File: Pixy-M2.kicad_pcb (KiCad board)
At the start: 4 copper layers, 66 x 100 mm, 78 parts, among them J1 USB_C_Receptacle_USB2.0_14P, J10 SM09B-SRSS-TB, J11 SM06B-SRSS-TB, J4 SM06B-SRSS-TB, J5 SM06B-SRSS-TB, J6 SM06B-SRSS-TB, J7 SM06B-SRSS-TB, J8 S6B-PH-K, J9 S6B-PH-K, Q1 AO4407A, SW1 SW_Push, SW2 SW_Push, SW3 JS102011SAQN, U1 ESP32-S3-WROOM-1-N16, U2 USBLC6-2SC6, U3 AP63203WU, U4 DRV8231ADSG, U5 DRV8231ADSG

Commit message: layout: shorten GPIO48 encoder route for audit P3
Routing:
- net /GPIO48: track 72.4 -> 26.0 mm

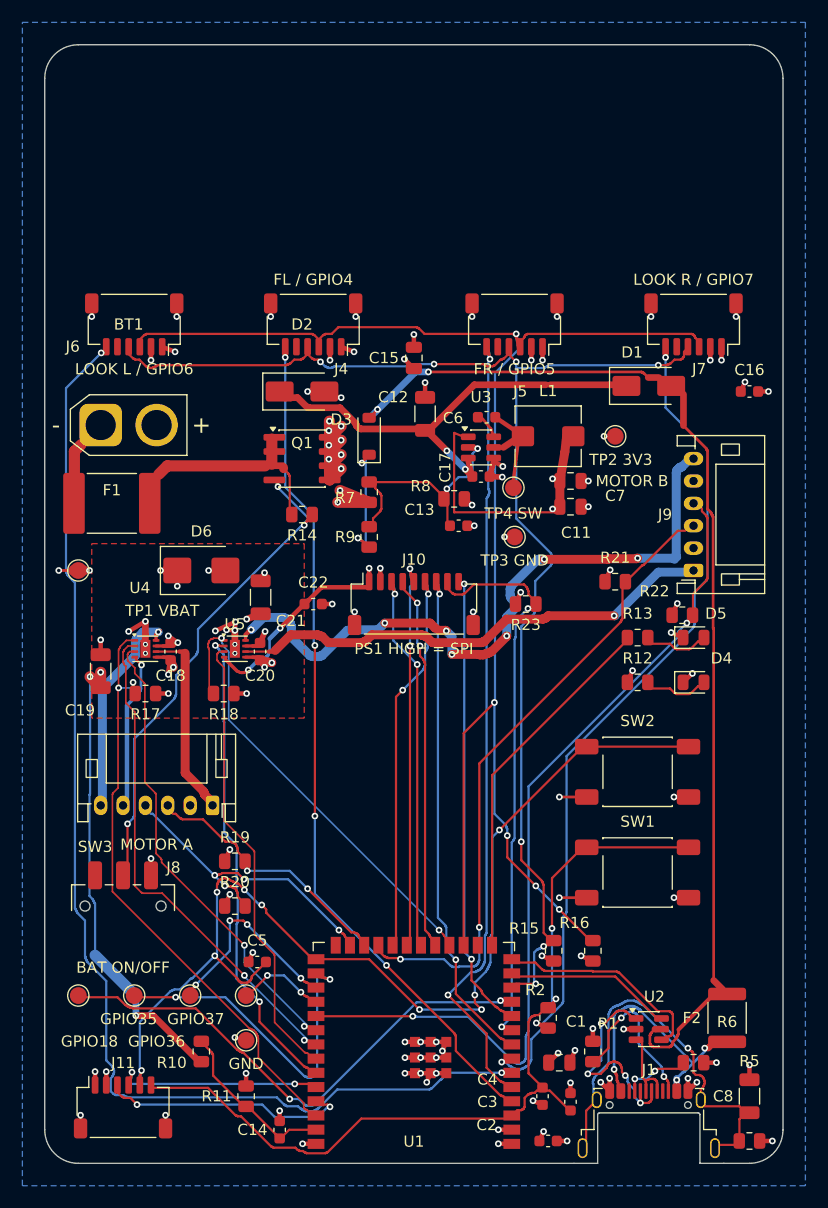
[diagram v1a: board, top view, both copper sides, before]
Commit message: layout: complete issue 6 drill clearance and thermal via treatment
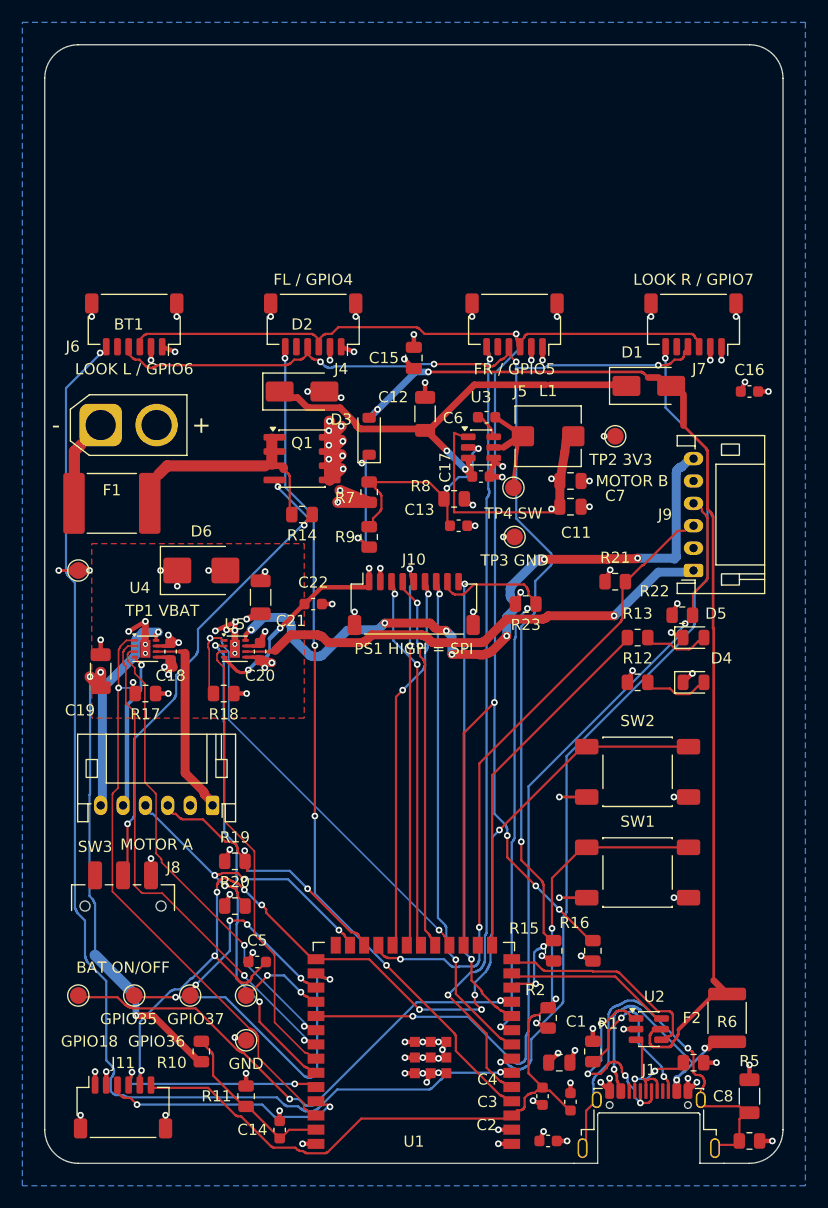
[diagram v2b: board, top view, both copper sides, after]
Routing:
- net /GPIO47: track 21.0 -> 24.6 mm
- net /GPIO10: track 40.7 -> 42.7 mm
- net GND: track 93.8 -> 95.8 mm
- net /VBAT: track 76.3 -> 77.6 mm
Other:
- board text added: "All other via drills clear pad mask and paste openings by >= 0.10 mm."
- board text added: "Fabrication order must include the specified filled/capped process."
- board text added: "IPC-4761 type VII is required; per-via filling and capping are enabled."
- board text added: "Resin fill and copper cap the four 0.25 mm thermal vias in U4/U5 pads."
- board text added: "These four vias lie under solder paste. Tenting is not a substitute."
- board text removed: "(IPC-4761 type VII). Confirm the option with the fabricator: tenting and"
- board text removed: "The four 0.25 mm vias inside the U4 and U5 exposed pads (DRV8231A) are"
- board text removed: "board lies inside a pad opening."
- board text removed: "filled/capped via-in-pad are different processes. No other via on this"
- board text removed: "thermal vias and sit under solder paste. They require resin fill and cap"
